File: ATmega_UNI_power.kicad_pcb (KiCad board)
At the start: 2 copper layers, 15.9 x 21.6 mm, 14 parts, among them J5 PWR_Jack, J9 Power_Conn, J91 Power_Conn, U53 LP2985-3.3, U55 AMS1117-5.0

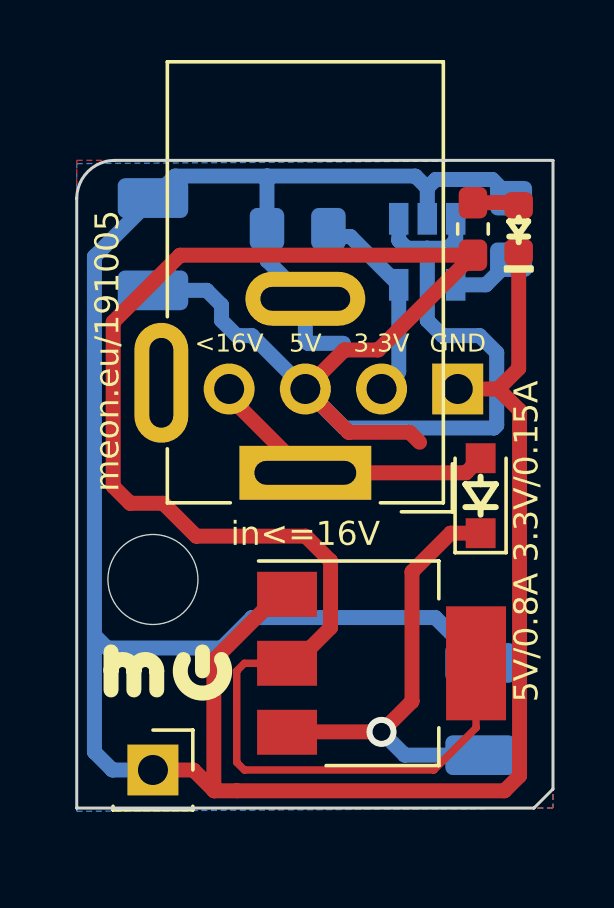
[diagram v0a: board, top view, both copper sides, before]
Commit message: make it 600x900 mils
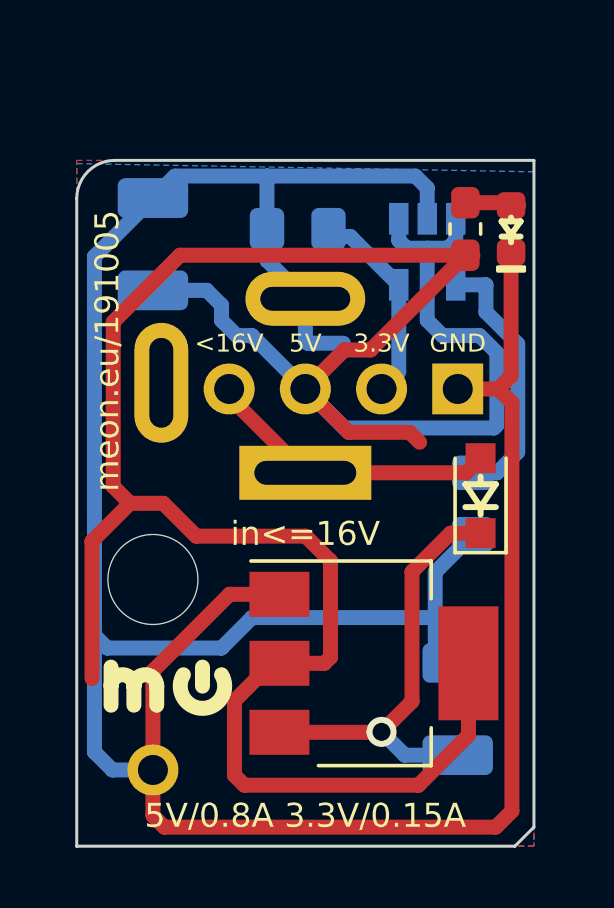
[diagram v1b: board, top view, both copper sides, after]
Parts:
- J5: footprint Connector_BarrelJack:BarrelJack_Wuerth_6941xx301002 -> Connector_BarrelJack:BarrelJack_Wuerth_6941xx301002_no_lines
- J91: footprint Connector_PinSocket_2.54mm:PinSocket_1x01_P2.54mm_Vertical -> Connector_PinHeader_2.54mm:PinHeader_1x01_P2.54mm_Vertical_no_lines
- U53: footprint Package_TO_SOT_SMD:SOT-23-5 -> Package_TO_SOT_SMD (GitHub):SOT-23-5_no_lines
- moved C55 9.24 mm to (170.7, 54.6), turned to 90 degrees
- moved C51 0.76 mm to (170.2, 61.5)
- moved REF** 0.51 mm to (160.5, 60.7)
- moved D9 0.25 mm to (172.0, 45.5)
- moved R9 0.25 mm to (170.4, 45.5)
- moved U55 0.25 mm to (167.4, 59.9)
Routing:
- net 5V: track 83.6 -> 91.1 mm
- net Net-(C55-Pad2): track 2.19 -> 8.80 mm
- net GND: track 96.9 -> 99.7 mm
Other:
- board size 15.9 x 21.6 mm -> 15.2 x 22.9 mm
- board text removed: "meon.eu/191005 5V/0.8A 3.3V/0.15A"

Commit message: remove power jack so it can go directly on a board below
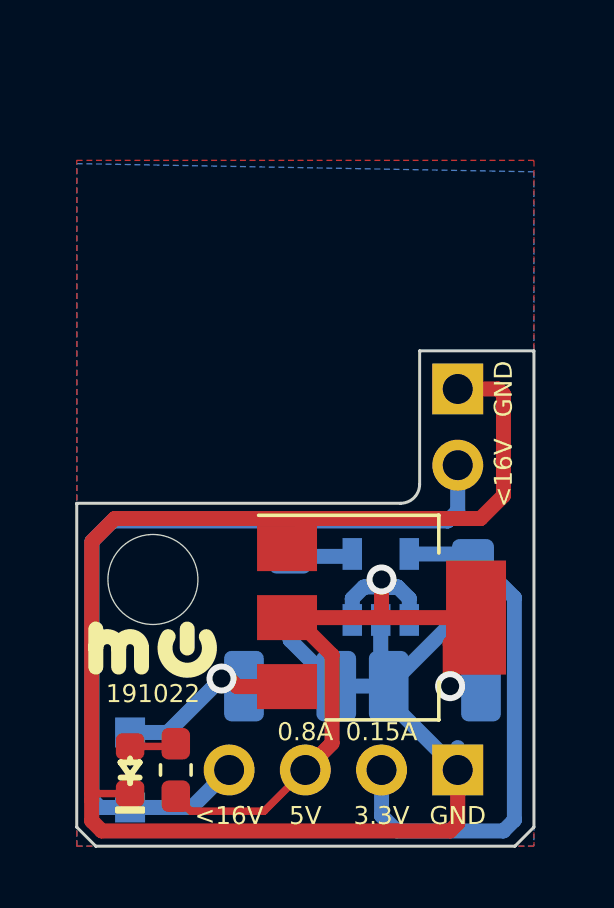
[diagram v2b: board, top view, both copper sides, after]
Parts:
- removed J5: PWR_Jack, Connector_BarrelJack:BarrelJack_Wuerth_6941xx301002_no_lines
- D5: moved to B.Cu
- J91: value Power_Conn -> RAW_Conn; footprint Connector_PinHeader_2.54mm:PinHeader_1x01_P2.54mm_Vertical_no_lines -> Connector_PinHeader_2.54mm:PinHeader_1x02_P2.54mm_Vertical_no_lines
- U53: footprint Package_TO_SOT_SMD (GitHub):SOT-23-5_no_lines -> Package_TO_SOT_SMD:SOT-23-5_no_lines
- moved D9 22.1 mm to (159.3, 63.5)
- moved R9 20.5 mm to (160.8, 63.5)
- moved C52 17.5 mm to (169.4, 60.7), turned to 180 degrees
- moved J91 16.3 mm to (170.2, 50.8)
- moved D5 14.8 mm to (159.3, 63.5), turned to 270 degrees
- moved C54 13.3 mm to (170.7, 57.4), turned to 90 degrees
- moved J9 12.7 mm to (170.2, 63.5)
- moved U53 11.3 mm to (167.6, 57.4), turned to 90 degrees
- moved C55 6.70 mm to (164.6, 57.4)
- moved C51 5.64 mm to (164.6, 60.7), turned to 0 degrees
- moved U55 1.55 mm to (167.6, 58.4)
- moved REF** 1.37 mm to (160.0, 59.4)
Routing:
- net 5V: track 91.1 -> 27.4 mm, vias 0 -> 2
- net GND: track 99.7 -> 60.7 mm
- net RAW_JACK: track 9.89 -> 27.9 mm
- net 3.3V: track 6.92 -> 17.8 mm
- net RAW: track 14.9 -> 6.58 mm
- net Net-(C55-Pad2): track 8.80 -> 2.10 mm
- net Net-(D9-Pad2): track 1.56 -> 2.19 mm
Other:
- board size 15.2 x 22.9 mm -> 15.2 x 16.5 mm
- board text added: "0.15A"
- board text added: "0.8A"
- board text added: "191022"
- board text removed: "5V/0.8A 3.3V/0.15A"
- board text removed: "in<=16V"
- board text removed: "meon.eu/191005"

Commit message: add jack back, but with break-away drills
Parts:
- added J1: Barrel_Jack_MountingPin, Connector_BarrelJack:BarrelJack_Wuerth_6941xx301002_no_lines, F.Cu at (163.8, 52.6)
- added J92: RAW_Conn, Connector_PinHeader_2.54mm:PinHeader_1x02_P2.54mm_Vertical_no_lines, F.Cu at (170.2, 48.3)
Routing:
- net Net-(J1-Pad2): track 0.00 -> 14.8 mm
- net Net-(J1-Pad1): track 0.00 -> 9.91 mm
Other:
- board size 15.2 x 16.5 mm -> 15.2 x 22.9 mm
- board text added: "191023"
- board text removed: "191022"

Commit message: adjust break-out holes
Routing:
- net Net-(J1-Pad2): track 14.8 -> 7.78 mm
- added copper zone on F.Cu, net Net-(J1-Pad1)
- added copper zone on B.Cu, net Net-(J1-Pad2)
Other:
- board size 15.2 x 22.9 mm -> 16.3 x 22.9 mm
- board text added: "191104"
- board text removed: "191023"
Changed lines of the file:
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@@
   (general
     (thickness 1.6)
-    (drawings 51)
-    (tracks 95)
+    (drawings 57)
+    (tracks 91)
     (zones 0)
     (modules 15)
@@
   )
   (setup
-    (last_trace_width 0.25)
+    (last_trace_width 0.5)
     (user_trace_width 0.25)
     (user_trace_width 0.5)
@@
     )
   )
-  (gr_arc (start 171.323 49.53) (end 171.323 49.657) (angle -180) (layer Edge.Cuts) (width 0.1))
-  (gr_arc (start 172.72 49.53) (end 172.72 49.022) (angle -180) (layer Edge.Cuts) (width 0.1))
-  (gr_arc (start 162.052 54.102) (end 162.052 54.356) (angle -180) (layer Edge.Cuts) (width 0.1))
-  (gr_arc (start 160.782 54.102) (end 160.782 53.848) (angle -180) (layer Edge.Cuts) (width 0.1))
-  (gr_line (start 162.052 53.848) (end 160.782 53.848) (layer Edge.Cuts) (width 0.1))
-  (gr_line (start 162.052 54.356) (end 160.782 54.356) (layer Edge.Cuts) (width 0.1))
-  (gr_arc (start 164.592 54.102) (end 164.592 54.356) (angle -180) (layer Edge.Cuts) (width 0.1))
-  (gr_line (start 164.592 54.356) (end 163.322 54.356) (layer Edge.Cuts) (width 0.1))
-  (gr_arc (start 163.322 54.102) (end 163.322 53.848) (angle -180) (layer Edge.Cuts) (width 0.1))
-  (gr_line (start 164.592 53.848) (end 163.322 53.848) (layer Edge.Cuts) (width 0.1))
-  (gr_arc (start 168.91 49.911) (end 168.91 49.657) (angle -90) (layer Edge.Cuts) (width 0.1))
+  (gr_line (start 168.148 54.102) (end 157.988 54.102) (layer F.SilkS) (width 0.5))
+  (gr_line (start 168.148 54.102) (end 157.988 54.102) (layer B.SilkS) (width 0.5))
+  (gr_line (start 172.212 49.53) (end 168.656 49.53) (layer B.SilkS) (width 0.5))
+  (gr_line (start 172.212 49.53) (end 168.656 49.53) (layer F.SilkS) (width 0.5))
+  (gr_circle (center 172.72 49.53) (end 173.228 49.53) (layer Edge.Cuts) (width 0.1))
+  (gr_circle (center 157.48 54.102) (end 157.988 54.102) (layer Edge.Cuts) (width 0.1))
+  (gr_arc (start 169.164 49.53) (end 169.164 49.276) (angle -180) (layer Edge.Cuts) (width 0.1))
+  (gr_arc (start 167.64 54.102) (end 167.64 54.356) (angle -180) (layer Edge.Cuts) (width 0.1))
+  (gr_line (start 160.02 54.356) (end 158.75 54.356) (layer Edge.Cuts) (width 0.1))
+  (gr_line (start 160.02 53.848) (end 158.75 53.848) (layer Edge.Cuts) (width 0.1))
+  (gr_arc (start 160.02 54.102) (end 160.02 54.356) (angle -180) (layer Edge.Cuts) (width 0.1))
+  (gr_arc (start 158.75 54.102) (end 158.75 53.848) (angle -180) (layer Edge.Cuts) (width 0.1))
+  (gr_arc (start 171.196 49.53) (end 171.196 49.784) (angle -180) (layer Edge.Cuts) (width 0.1))
+  (gr_line (start 171.196 49.784) (end 169.164 49.784) (layer Edge.Cuts) (width 0.1))
+  (gr_line (start 171.196 49.276) (end 169.164 49.276) (layer Edge.Cuts) (width 0.1))
+  (gr_arc (start 162.56 54.102) (end 162.56 54.356) (angle -180) (layer Edge.Cuts) (width 0.1))
+  (gr_arc (start 161.29 54.102) (end 161.29 53.848) (angle -180) (layer Edge.Cuts) (width 0.1))
+  (gr_line (start 162.56 53.848) (end 161.29 53.848) (layer Edge.Cuts) (width 0.1))
+  (gr_line (start 162.56 54.356) (end 161.29 54.356) (layer Edge.Cuts) (width 0.1))
+  (gr_arc (start 165.1 54.102) (end 165.1 54.356) (angle -180) (layer Edge.Cuts) (width 0.1))
+  (gr_line (start 165.1 54.356) (end 163.83 54.356) (layer Edge.Cuts) (width 0.1))
+  (gr_arc (start 163.83 54.102) (end 163.83 53.848) (angle -180) (layer Edge.Cuts) (width 0.1))
+  (gr_line (start 165.1 53.848) (end 163.83 53.848) (layer Edge.Cuts) (width 0.1))
   (gr_text <16V (at 171.704 45.72 90) (layer F.SilkS)
     (effects (font (size 0.6 0.6) (thickness 0.125)))
@@
     (effects (font (size 0.6 0.6) (thickness 0.125)) (justify mirror))
   )
-  (gr_line (start 167.132 53.848) (end 165.862 53.848) (layer Edge.Cuts) (width 0.1))
-  (gr_line (start 167.132 54.356) (end 165.862 54.356) (layer Edge.Cuts) (width 0.1))
-  (gr_arc (start 165.862 54.102) (end 165.862 53.848) (angle -180) (layer Edge.Cuts) (width 0.1))
-  (gr_arc (start 167.132 54.102) (end 167.132 54.356) (angle -180) (layer Edge.Cuts) (width 0.1))
+  (gr_line (start 167.64 53.848) (end 166.37 53.848) (layer Edge.Cuts) (width 0.1))
+  (gr_line (start 167.64 54.356) (end 166.37 54.356) (layer Edge.Cuts) (width 0.1))
+  (gr_arc (start 166.37 54.102) (end 166.37 53.848) (angle -180) (layer Edge.Cuts) (width 0.1))
   (gr_arc (start 168.402 54.102) (end 168.148 54.102) (angle -180) (layer Edge.Cuts) (width 0.1))
   (gr_line (start 168.148 49.657) (end 168.148 54.102) (layer Edge.Cuts) (width 0.1))
-  (gr_line (start 168.656 49.911) (end 168.656 54.102) (layer Edge.Cuts) (width 0.1))
-  (gr_arc (start 168.402 49.657) (end 168.402 49.403) (angle -90) (layer Edge.Cuts) (width 0.1))
-  (gr_line (start 172.72 49.022) (end 172.72 43.18) (layer Edge.Cuts) (width 0.1))
-  (gr_line (start 157.48 53.594) (end 157.48 44.45) (layer Edge.Cuts) (width 0.1))
-  (gr_arc (start 157.48 54.102) (end 157.48 54.61) (angle -180) (layer Edge.Cuts) (width 0.1))
+  (gr_line (start 168.656 49.657) (end 168.656 54.102) (layer Edge.Cuts) (width 0.1))
+  (gr_arc (start 168.402 49.657) (end 168.656 49.657) (angle -180) (layer Edge.Cuts) (width 0.1))
   (gr_arc (start 158.75 44.45) (end 158.75 43.18) (angle -90) (layer Edge.Cuts) (width 0.1))
   (gr_text GND (at 171.704 48.133 90) (layer F.SilkS)
@@
     (effects (font (size 0.6 0.6) (thickness 0.125)) (justify mirror))
   )
-  (gr_line (start 168.91 49.657) (end 171.323 49.657) (layer Edge.Cuts) (width 0.1))
   (gr_line (start 172.72 43.18) (end 158.75 43.18) (layer Edge.Cuts) (width 0.1))
-  (gr_line (start 168.402 49.403) (end 171.323 49.403) (layer Edge.Cuts) (width 0.1))
   (gr_text GND (at 171.704 50.927 90) (layer B.SilkS)
     (effects (font (size 0.6 0.6) (thickness 0.125)) (justify mirror))
@@
   )
   (gr_line (start 157.48 65.405) (end 158.115 66.04) (layer Edge.Cuts) (width 0.1))
-  (gr_text 191023 (at 160.02 60.96) (layer B.SilkS)
+  (gr_text 191104 (at 160.02 60.96) (layer B.SilkS)
     (effects (font (size 0.6 0.6) (thickness 0.125)) (justify mirror))
   )
@@
   )
   (gr_line (start 172.085 66.04) (end 172.72 65.405) (layer Edge.Cuts) (width 0.1))
-  (gr_text 191023 (at 160.02 60.96) (layer F.SilkS)
-    (effects (font (size 0.6 0.6) (thickness 0.125)))
-  )
-  (gr_line (start 157.48 65.405) (end 157.48 54.61) (layer Edge.Cuts) (width 0.1))
+  (gr_text 191104 (at 160.02 60.96) (layer F.SilkS)
+    (effects (font (size 0.6 0.6) (thickness 0.125)))
+  )
+  (gr_line (start 157.48 65.405) (end 157.48 44.45) (layer Edge.Cuts) (width 0.1))
   (gr_line (start 172.085 66.04) (end 158.115 66.04) (layer Edge.Cuts) (width 0.1))
-  (gr_line (start 172.72 50.038) (end 172.72 65.405) (layer Edge.Cuts) (width 0.1))
+  (gr_line (start 172.72 43.18) (end 172.72 65.405) (layer Edge.Cuts) (width 0.1))
   (segment (start 162.56 60.452) (end 163.3085 60.452) (width 0.5) (layer B.Cu) (net 1) (status 20))
   (via (at 162.306 60.452) (size 1) (drill 0.6) (layers F.Cu B.Cu) (net 1))
@@
   (segment (start 160.6945 62.7125) (end 160.782 62.625) (width 0.25) (layer F.Cu) (net 7) (status 30))
   (segment (start 159.258 62.7125) (end 160.6945 62.7125) (width 0.25) (layer F.Cu) (net 7) (status 30))
-  (segment (start 171.53 48.26) (end 170.18 48.26) (width 0.5) (layer F.Cu) (net 8))
-  (segment (start 163.83 46.524) (end 163.83 45.124) (width 0.5) (layer F.Cu) (net 8))
-  (segment (start 164.758 44.196) (end 171.196 44.196) (width 0.5) (layer F.Cu) (net 8))
-  (segment (start 171.704 44.704) (end 171.704 48.086) (width 0.5) (layer F.Cu) (net 8))
-  (segment (start 163.83 45.124) (end 164.758 44.196) (width 0.5) (layer F.Cu) (net 8))
-  (segment (start 171.196 44.196) (end 171.704 44.704) (width 0.5) (layer F.Cu) (net 8))
-  (segment (start 171.704 48.086) (end 171.53 48.26) (width 0.5) (layer F.Cu) (net 8))
+  (segment (start 163.83 48.178) (end 163.83 46.778) (width 0.5) (layer B.Cu) (net 8))
+  (segment (start 163.912 48.26) (end 163.83 48.178) (width 0.5) (layer B.Cu) (net 8))
+  (segment (start 170.18 48.26) (end 163.912 48.26) (width 0.5) (layer B.Cu) (net 8))
   (segment (start 163.83 50.924) (end 169.034 45.72) (width 0.5) (layer F.Cu) (net 9))
   (segment (start 163.83 52.324) (end 163.83 50.924) (width 0.5) (layer F.Cu) (net 9))
@@
     (polygon
       (pts
-        (xy 157.48 43.18) (xy 172.72 43.18) (xy 172.72 66.04) (xy 157.48 66.04)
+        (xy 172.72 49.53) (xy 172.72 66.04) (xy 157.48 66.04) (xy 157.48 54.102) (xy 168.402 54.102)
+        (xy 168.402 49.53)
+      )
+    )
+  )
+  (zone (net 8) (net_name "Net-(J1-Pad2)") (layer B.Cu) (hatch edge 0.508)
+    (connect_pads (clearance 0.508))
+    (min_thickness 0.254)
+    (fill yes (arc_segments 16) (thermal_gap 0.508) (thermal_bridge_width 0.508))
+    (polygon
+      (pts
+        (xy 157.48 43.18) (xy 172.72 43.18) (xy 172.72 49.53) (xy 168.402 49.53) (xy 168.402 54.102)
+        (xy 157.48 54.102)
+      )
+    )
+  )
+  (zone (net 9) (net_name "Net-(J1-Pad1)") (layer F.Cu) (hatch edge 0.508)
+    (connect_pads (clearance 0.508))
+    (min_thickness 0.254)
+    (fill yes (arc_segments 16) (thermal_gap 0.508) (thermal_bridge_width 0.508))
+    (polygon
+      (pts
+        (xy 157.48 43.18) (xy 172.72 43.18) (xy 172.72 49.53) (xy 168.402 49.53) (xy 168.402 54.102)
+        (xy 157.48 54.102)
       )
     )
@@
     (polygon
       (pts
-        (xy 157.48 43.18) (xy 172.72 43.18) (xy 172.72 66.04) (xy 157.48 66.04)
+        (xy 172.72 66.04) (xy 157.48 66.04) (xy 157.48 54.102) (xy 172.72 54.102)
       )
     )

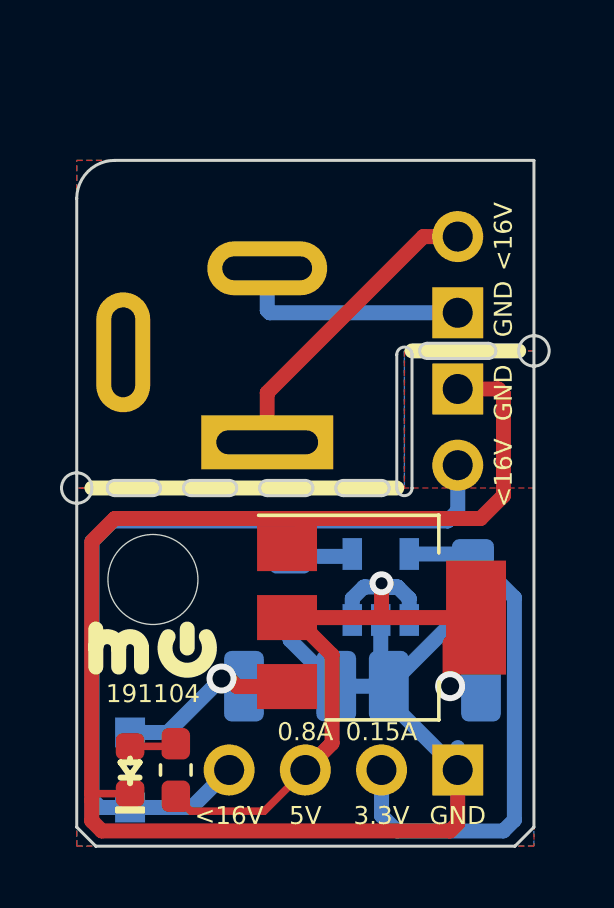
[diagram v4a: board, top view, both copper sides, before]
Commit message: use ams1117 also for 3.3V, rm led power-on indication
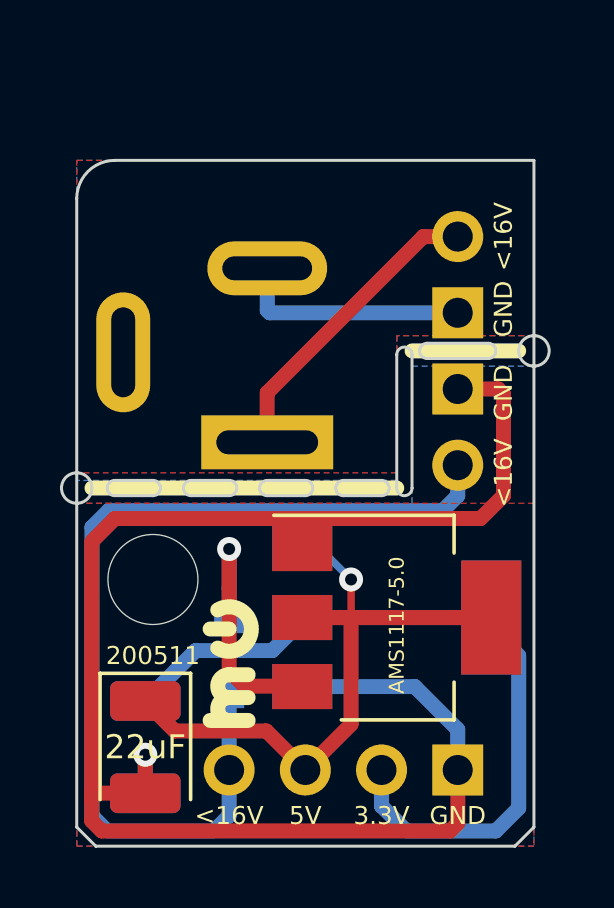
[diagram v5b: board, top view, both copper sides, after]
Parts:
- removed C51: 10uF, Capacitor_Tantalum_SMD:CP_EIA-3528-21_Kemet-B
- removed C54: 2.2uF, Capacitor_SMD:C_0805_2012Metric_Pad1.15x1.40mm_HandSolder
- removed C55: 0.01uF, Capacitor_SMD:C_0805_2012Metric_Pad1.15x1.40mm_HandSolder
- removed D9: PWR, LED_SMD.debian:LED_0603_1608Metric_symbol
- removed R9: 1k, Resistor_SMD:R_0603_1608Metric_Pad1.05x0.95mm_HandSolder
- removed U53: LP2985-3.3, Package_TO_SOT_SMD:SOT-23-5_no_lines
- added C32: 22uF, Capacitor_Tantalum_SMD:CP_EIA-3528-21_Kemet-B, B.Cu at (159.8, 62.7)
- added U33: AMS1117-3.3, Package_TO_SOT_SMD:SOT-223-3_TabPin2, B.Cu at (168.1, 58.4)
- C52: value 10uF -> 22uF; moved to F.Cu
- REF**: value mo-logo-small -> mo-logo-small-on-side; footprint meon:mo-logo-small -> meon:mo-logo-small-on-side
- moved C52 9.86 mm to (159.8, 62.7), turned to 270 degrees
- moved D5 5.04 mm to (162.6, 59.7)
- moved REF** 2.59 mm to (162.6, 59.9), turned to 90 degrees
- moved U55 0.51 mm to (168.1, 58.4)
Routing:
- net 3.3V: track 17.8 -> 25.9 mm
- net 5V: track 27.3 -> 21.8 mm, vias 2 -> 1
- net GND: track 60.7 -> 55.7 mm, vias 0 -> 1
- net RAW_JACK: track 27.9 -> 31.8 mm
- net RAW: track 6.58 -> 8.87 mm
- net Net-(D9-Pad2): track 2.19 -> 0.00 mm
- net Net-(C55-Pad2): track 2.10 -> 0.00 mm
- added copper zone on B.Cu, net 3.3V
- removed copper zone on B.Cu, net GND
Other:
- board text added: "200511"
- board text removed: "0.15A"
- board text removed: "0.8A"
- board text removed: "191104"
